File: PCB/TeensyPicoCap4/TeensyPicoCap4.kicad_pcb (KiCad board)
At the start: 2 copper layers, 77.5 x 63.5 mm, 42 parts, among them J1 Conn_01x02, J10 Conn_01x01_Male, J11 Conn_01x01_Male, J12 Conn_01x01_Male, J13 Conn_01x01_Male, J14 Conn_01x24, J15 Conn_01x24, J16 Barrel_Jack_Switch_Pin3Ring, J17 Conn_01x08, J18 Conn_01x08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

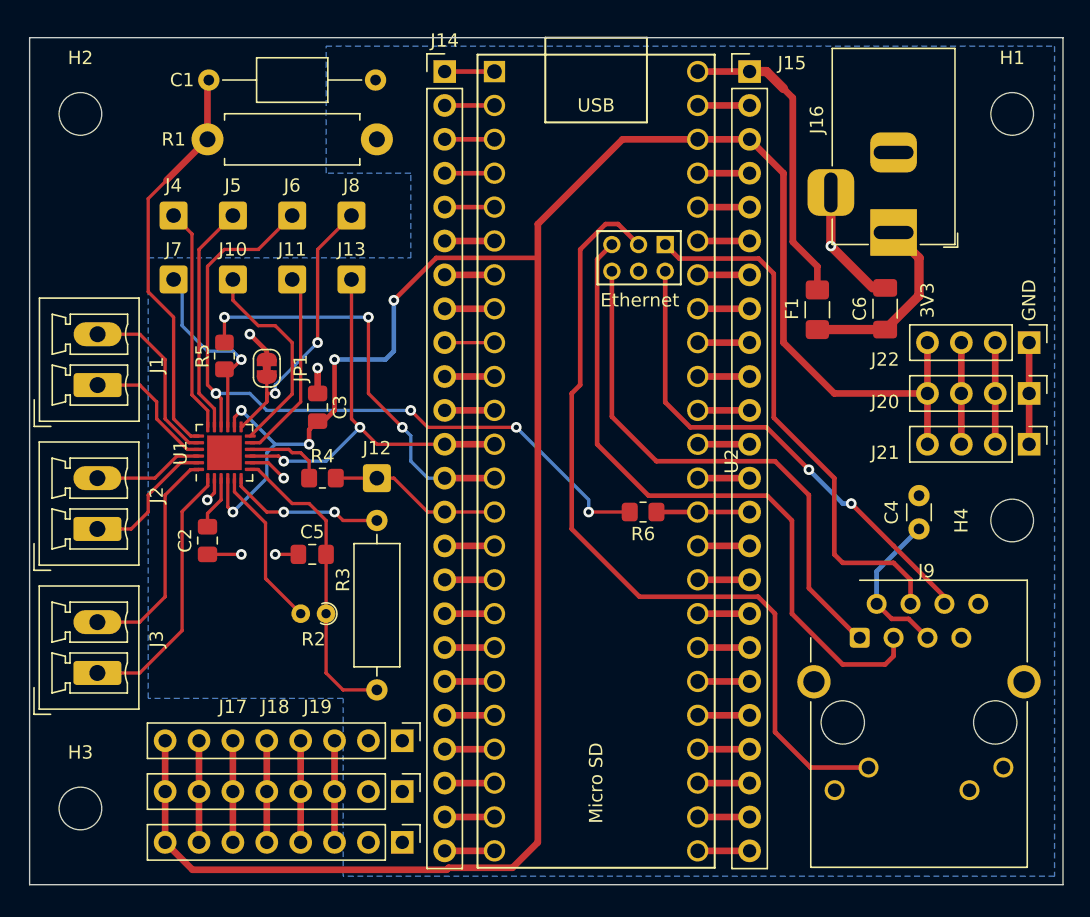
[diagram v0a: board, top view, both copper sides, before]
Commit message: submitted V1 w/ more silk and digikey parts
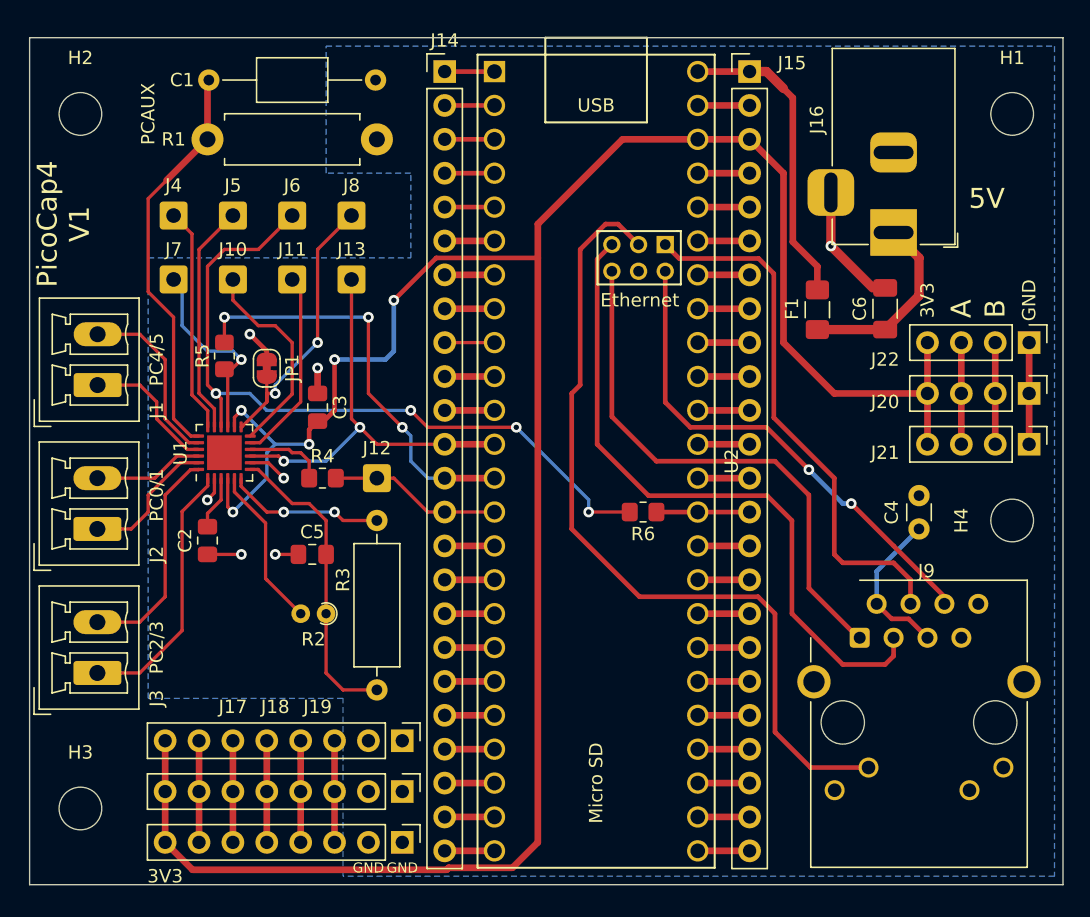
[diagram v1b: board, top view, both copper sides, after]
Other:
- board text added: "5V"
- board text added: "A"
- board text added: "B"
- board text added: "PC0/1"
- board text added: "PC2/3"
- board text added: "PC4/5"
- board text added: "PCAUX"
- board text added: "PicoCap4 V1"
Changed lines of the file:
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@@
     (property "Sheetname" "")
     (attr exclude_from_pos_files)
-    (fp_text reference "JP1" (at 0 2.54 90) (layer "F.SilkS")
+    (fp_text reference "JP1" (at 0.015 1.905 90) (layer "F.SilkS")
       (effects (font (size 1 1) (thickness 0.15)))
     )
@@
     (property "Sheetname" "")
     (attr through_hole)
-    (fp_text reference "J2" (at 2.54 4.445 90) (layer "F.SilkS")
+    (fp_text reference "J2" (at -1.905 4.445 90) (layer "F.SilkS")
       (effects (font (size 1 1) (thickness 0.15)))
     )
@@
     (property "Sheetname" "")
     (attr through_hole)
-    (fp_text reference "J3" (at 2.54 4.445 90) (layer "F.SilkS")
+    (fp_text reference "J3" (at -1.905 4.445 90) (layer "F.SilkS")
       (effects (font (size 1 1) (thickness 0.15)))
     )
@@
     (property "Sheetname" "")
     (attr through_hole)
-    (fp_text reference "J1" (at 1.5 4.4275 90) (layer "F.SilkS")
+    (fp_text reference "J1" (at -1.8975 4.4275 90) (layer "F.SilkS")
       (effects (font (size 1 1) (thickness 0.15)))
     )
@@
   (gr_line (start 220.98 53.34) (end 220.98 116.84) (layer "Edge.Cuts") (width 0.1))
   (gr_line (start 143.51 116.84) (end 143.51 53.34) (layer "Edge.Cuts") (width 0.1))
+  (gr_text "PC0/1" (at 153.035 87.63 90) (layer "F.SilkS")
+    (effects (font (size 1 1) (thickness 0.15)))
+  )
+  (gr_text "PC4/5" (at 153.035 77.47 90) (layer "F.SilkS")
+    (effects (font (size 1 1) (thickness 0.15)))
+  )
+  (gr_text "5V" (at 215.265 65.405) (layer "F.SilkS")
+    (effects (font (size 1.5 1.5) (thickness 0.3)))
+  )
+  (gr_text "GND" (at 168.91 115.57) (layer "F.SilkS")
+    (effects (font (size 0.75 0.75) (thickness 0.15)))
+  )
+  (gr_text "B" (at 215.9 73.66 90) (layer "F.SilkS")
+    (effects (font (size 1.5 1.5) (thickness 0.3)))
+  )
   (gr_text "GND" (at 218.44 73.025 90) (layer "F.SilkS")
     (effects (font (size 1 1) (thickness 0.15)))
   )
+  (gr_text "PCAUX" (at 152.4 59.055 90) (layer "F.SilkS")
+    (effects (font (size 1 1) (thickness 0.15)))
+  )
+  (gr_text "PC2/3" (at 153.035 99.06 90) (layer "F.SilkS")
+    (effects (font (size 1 1) (thickness 0.15)))
+  )
+  (gr_text "A" (at 213.36 73.66 90) (layer "F.SilkS")
+    (effects (font (size 1.5 1.5) (thickness 0.3)))
+  )
+  (gr_text "PicoCap4\nV1" (at 146.05 67.31 90) (layer "F.SilkS")
+    (effects (font (size 1.5 1.5) (thickness 0.3)))
+  )
+  (gr_text "3V3" (at 153.67 116.205) (layer "F.SilkS")
+    (effects (font (size 1 1) (thickness 0.15)))
+  )
   (gr_text "3V3" (at 210.82 73.025 90) (layer "F.SilkS")
     (effects (font (size 1 1) (thickness 0.15)))
   )
+  (gr_text "GND" (at 171.45 115.57) (layer "F.SilkS")
+    (effects (font (size 0.75 0.75) (thickness 0.15)))
+  )
   (segment (start 152.4 65.405) (end 153.77 64.035) (width 0.25) (layer "F.Cu") (net 1))
